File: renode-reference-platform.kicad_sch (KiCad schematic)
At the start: 33 parts, among them J1 USB-C_GCT_USB4105-GF-A, J2 USB-C_GCT_USB4105-GF-A, J3 RJ45_Abracon_ARJM11B1-502-AB-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, J4 Tag-Connect_TC2050-IDC-NL_2x5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, J5 PinSocket_2x6_P2.54mm_Drill1.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, J6 PinSocket_2x6_P2.54mm_Drill1.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, J7 PinSocket_2x20_P2.54mm_Drill1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, J8 JST_SH_1x4_SM04B-SRSS-TB-LF-SN, J9 JST_SH_1x4_SM04B-SRSS-TB-LF-SN, SW1 SW_1301_9305_THT, SW2 SW_1301_9305_THT, SW3 SW_1301_9305_THT, SW4 SW_1301_9305_THT, U1 STM32H753ZIT6, U2 FT2232HL-REEL, U3 IIS2MDCTR, U4 LSM6DSO32TR, U5 TMP108AIYFFR, U6 BME280, U7 AT25FF161A-MAHN-T, U8 INA187A1IDBVR

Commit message: [#94684] Add subsheets
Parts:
- removed D1, D2, D3, D4: LED_G_0402_VLMTG1500-GS08, antmicro-footprints:LED_0402_1005Metric_G, symbol antmicroLEDIndicationDiscrete:LED_G_0402_VLMTG1500-GS08
- removed D5: LED_RGB_2525_LTRBRASF_6B6C-0112-0, antmicro-footprints:LED_RGB_2525Metric_LTRBRASF, symbol antmicroLEDIndicationDiscrete:LED_RGB_2525_LTRBRASF_6B6C-0112-0
- removed J1, J2: USB-C_GCT_USB4105-GF-A, antmicro-footprints:USB-C_Receptacle_GCT_USB4105-GF-A, symbol antmicroUSBConnectors:USB-C_GCT_USB4105-GF-A
- removed J3: RJ45_Abracon_ARJM11B1-502-AB-EW2, antmicro-footprints:RJ45_ARJM11B1-502-AB-EW2_Horizontal, symbol antmicroModularConnectorsJacks:RJ45_Abracon_ARJM11B1-502-AB-EW2
- removed J4: Tag-Connect_TC2050-IDC-NL_2x5_P1.27mm, antmicro-footprints:Tag-Connect_TC2050-IDC-NL_2x5_P1.27mm, symbol antmicroTestPoints:Tag-Connect_TC2050-IDC-NL_2x5_P1.27mm
- removed J5, J6: PinSocket_2x6_P2.54mm_Drill1.04mm_Horizontal, antmicro-footprints:PinSocket_2x6_P2.54mm_Drill1.04mm_Horizontal, symbol antmicroGenericPinSockets:PinSocket_2x6_P2.54mm_Drill1.04mm_Horizontal
- removed J7: PinSocket_2x20_P2.54mm_Drill1.02mm, antmicro-footprints:PinSocket_2x20_P2.54mm_Drill1.02mm, symbol antmicroGenericPinSockets:PinSocket_2x20_P2.54mm_Drill1.02mm
- removed J8, J9: JST_SH_1x4_SM04B-SRSS-TB-LF-SN, antmicro-footprints:Conn_JST_SH_1x4_SM04B-SRSS-TB-LF-SN, symbol antmicroWire2BoardConnectors:JST_SH_1x4_SM04B-SRSS-TB-LF-SN
- removed R1, R2, R3: R_0R_0402, antmicro-footprints:R_0402_1005Metric, symbol antmicroResistors0402:R_0R_0402
- removed SW1, SW2, SW3, SW4: SW_1301_9305_THT, antmicro-footprints:SW_1301_9305_THT, symbol antmicroPushbuttonSwitches:SW_1301_9305_THT
- removed U1: STM32H753ZIT6, antmicro-footprints:LQFP-144_20x20mm_P0.5mm, symbol antmicroMicrocontrollers:STM32H753ZIT6
- removed U2: FT2232HL-REEL, antmicro-footprints:LQFP-64_10x10mm_P0.5mm, symbol antmicroInterfaceControllers:FT2232HL-REEL
- removed U3: IIS2MDCTR, antmicro-footprints:LGA-12_2x2mm_P0.5mm, symbol antmicroMotionSensorsIMUsInertialMeasurementUnits:IIS2MDCTR
- removed U4: LSM6DSO32TR, antmicro-footprints:LGA-14L_3x2.5mm_P0.5mm, symbol antmicroMotionSensorsIMUsInertialMeasurementUnits:LSM6DSO32TR
- removed U5: TMP108AIYFFR, antmicro-footprints:Texas_DSBGA-6_1.2x0.8mm_Layout2x3_P0.4mm, symbol antmicroTemperatureSensorsAnalogandDigitalOutput:TMP108AIYFFR
- removed U6: BME280, antmicro-footprints:LGA-8_2.5x2.5mm_BME280, symbol antmicroHumidityMoistureSensors:BME280
- removed U7: AT25FF161A-MAHN-T, antmicro-footprints:USON-8_2x3mm_P0.5mm, symbol antmicroMemory:AT25FF161A-MAHN-T
- removed U8: INA187A1IDBVR, antmicro-footprints:SOT-23-6, symbol antmicroPowerMeasurement:INA187A1IDBVR
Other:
- added sheet Ethernet (eth.kicad_sch)
- added sheet IMU (imu.kicad_sch)
- added sheet IOs (ios.kicad_sch)
- added sheet MCU (mcu.kicad_sch)
- added sheet PMOD (pmod.kicad_sch)
- added sheet Power (power.kicad_sch)
- added sheet RPI Connector (rpi-expansion.kicad_sch)
- added sheet SPI Flash (spi-flash.kicad_sch)
- added sheet USB-C (usb-c.kicad_sch)
- added sheet USB-C Debug (debug-usb-c.kicad_sch)

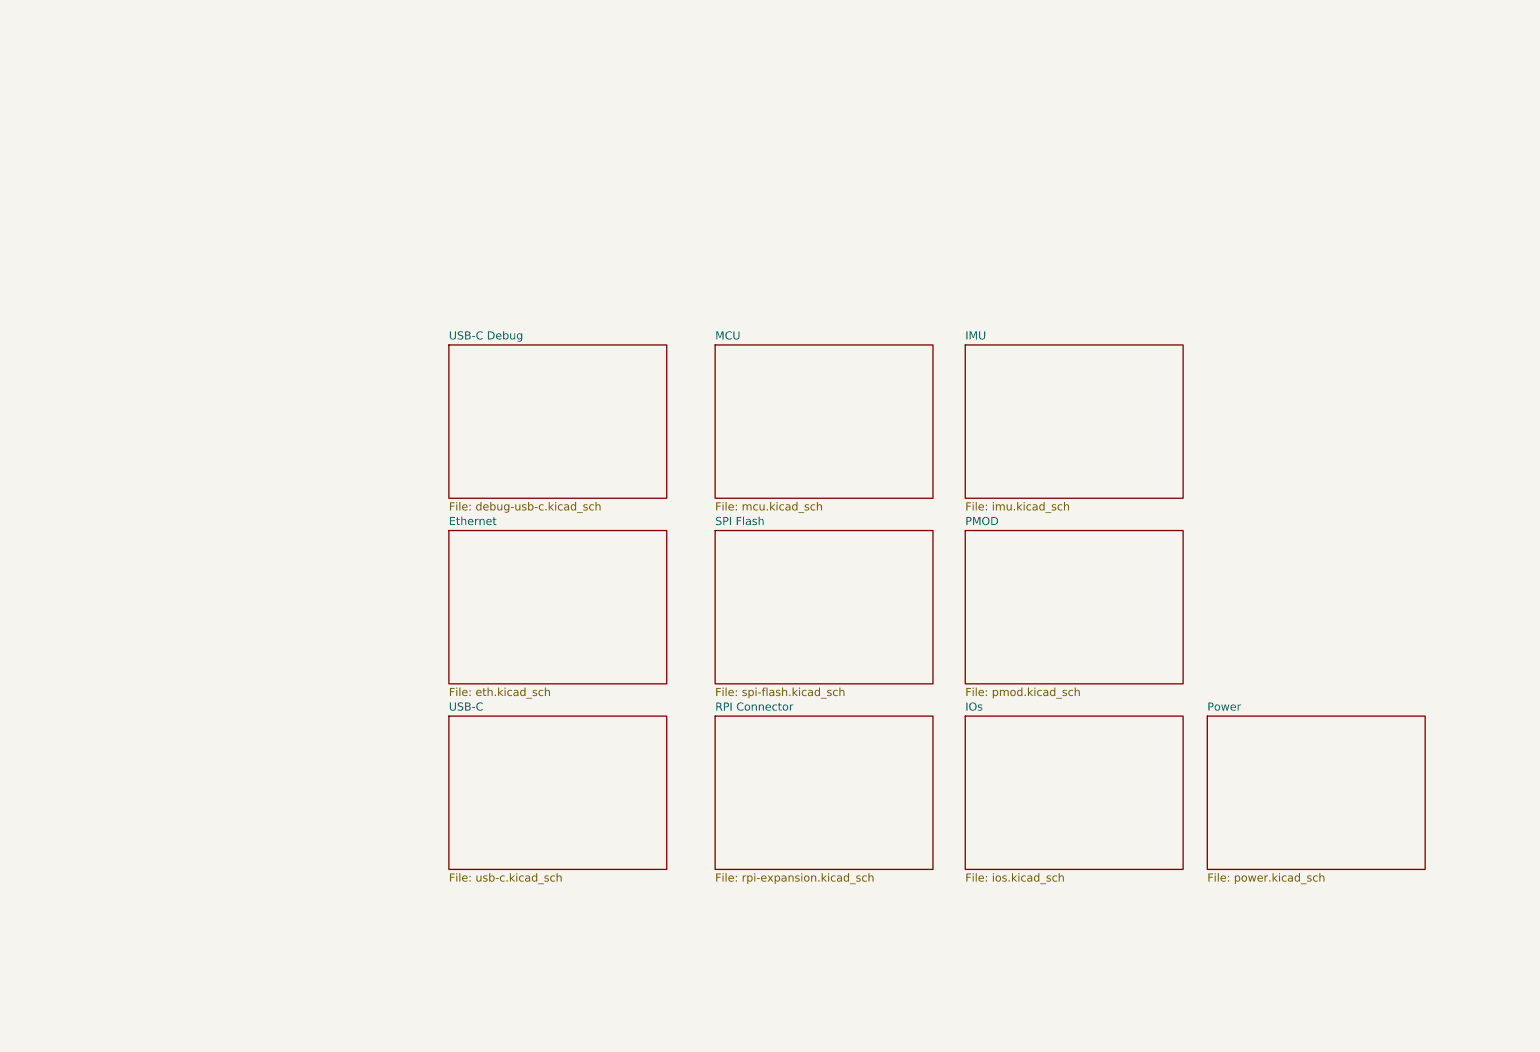
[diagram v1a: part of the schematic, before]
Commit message: [#94684] Add ports to subsheets
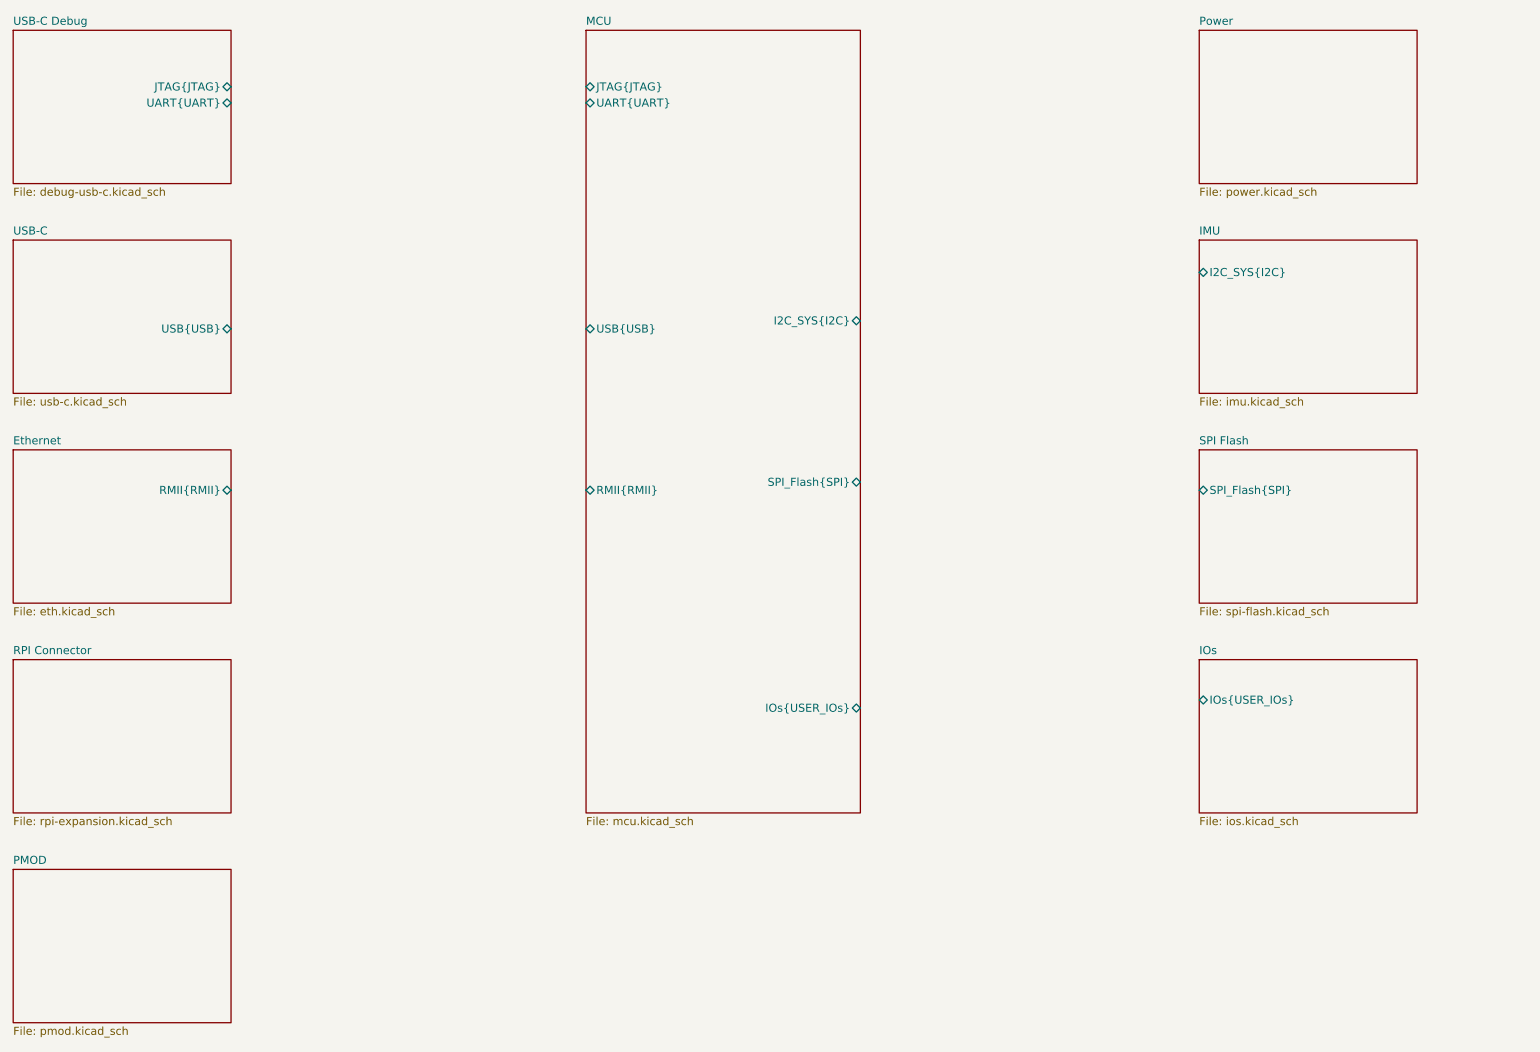
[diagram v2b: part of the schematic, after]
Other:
- sheet Ethernet ports: added RMII{RMII}; removed none
- sheet IMU ports: added I2C_SYS{I2C}; removed none
- sheet IOs ports: added IOs{USER_IOs}; removed none
- sheet MCU ports: added I2C_SYS{I2C}, IOs{USER_IOs}, JTAG{JTAG}, RMII{RMII}, SPI_Flash{SPI}, UART{UART}, USB{USB}; removed none
- sheet SPI Flash ports: added SPI_Flash{SPI}; removed none
- sheet USB-C ports: added USB{USB}; removed none
- sheet USB-C Debug ports: added JTAG{JTAG}, UART{UART}; removed none

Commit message: [#94684] Revise component placement
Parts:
- removed MP1, MP2, MP3, MP4: MP_NPTH_Drill3.2mm, antmicro-footprints:MP_NPTH_Drill3.2mm, symbol antmicroMechanicalParts:MP_NPTH_Drill3.2mm
- added MP1, MP2, MP3, MP4: MP_NPTH_Drill2.7mm, antmicro-footprints:MP_NPTH_Drill2.7mm, symbol antmicroMechanicalParts:MP_NPTH_Drill2.7mm

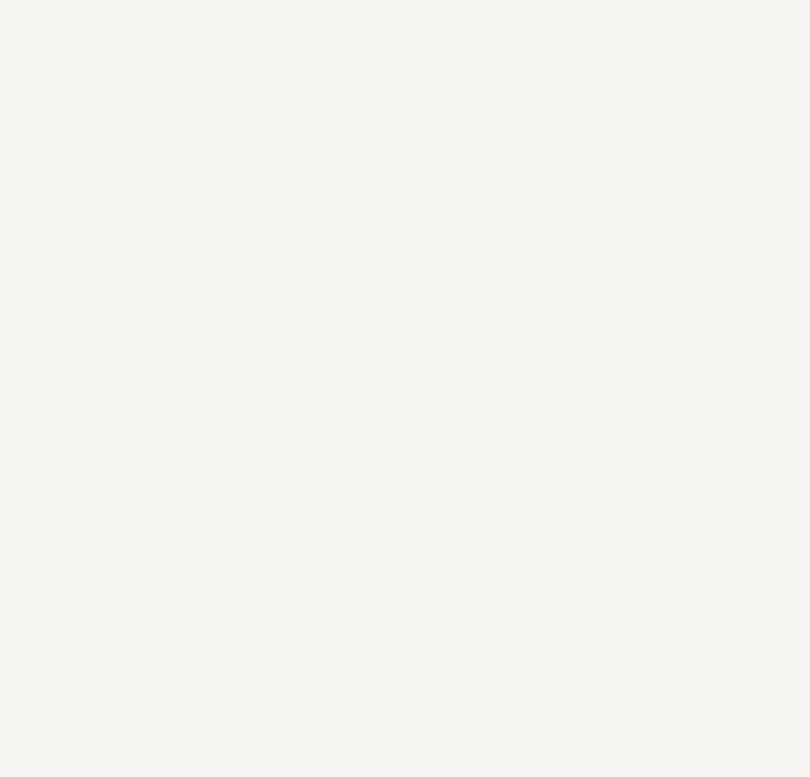
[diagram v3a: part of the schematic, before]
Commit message: [#94620] Add testpoints
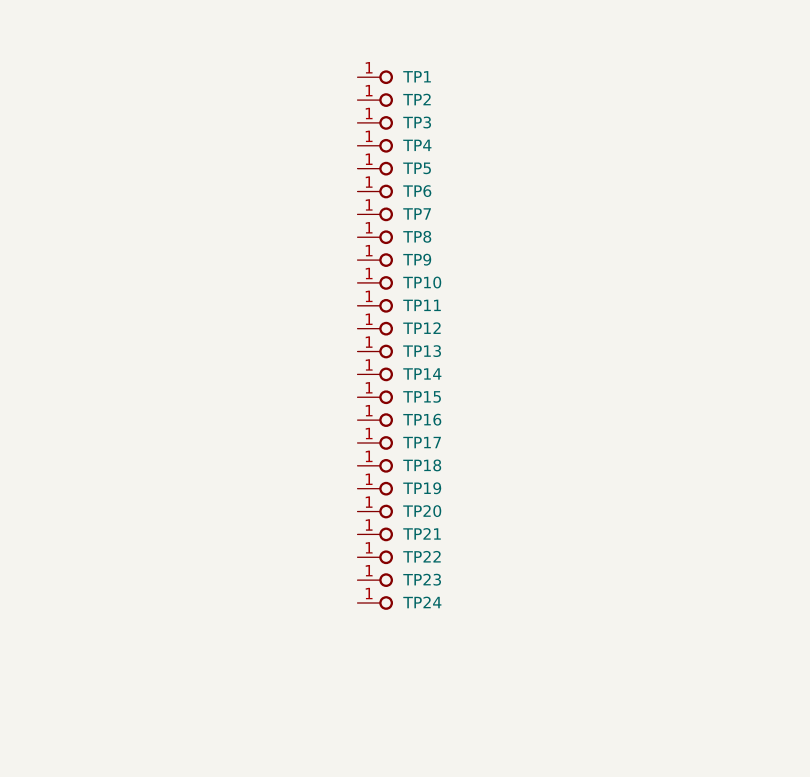
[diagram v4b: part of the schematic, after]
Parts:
- added TP1, TP10, TP11, TP12, TP13, TP14, TP15, TP16, TP17, TP18, TP19, TP2, TP20, TP21, TP22, TP23, TP24, TP3, TP4, TP5, TP6, TP7, TP8, TP9: TP_1.5mm_SMD, antmicro-footprints:TP_SMD_1.5mm, symbol antmicroTestPoints:TP_1.5mm_SMD

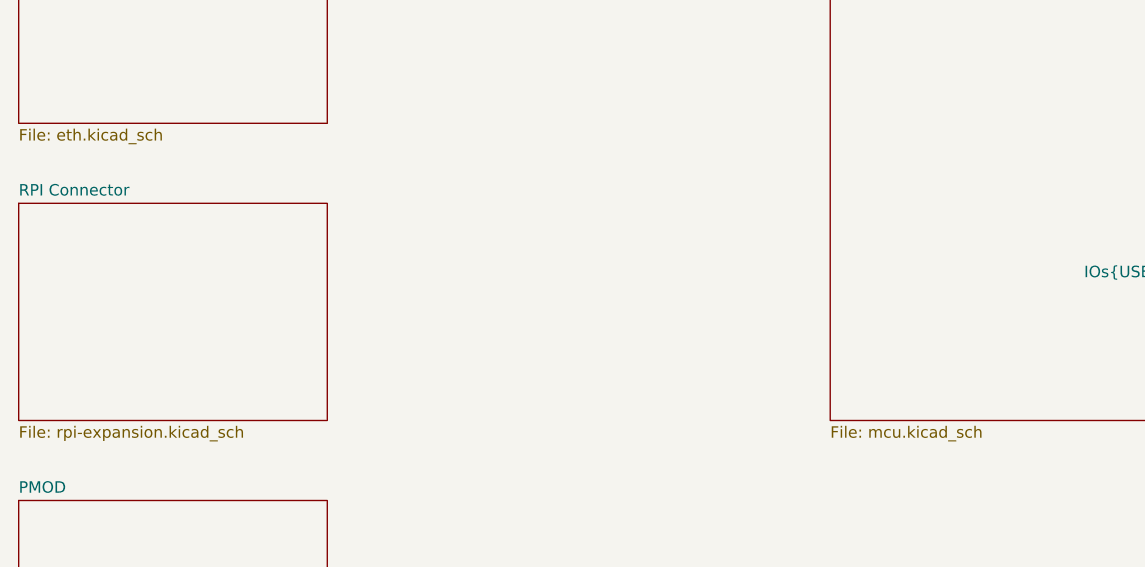
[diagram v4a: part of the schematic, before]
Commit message: [#94727] Add RMII, IOs, JTAG, UART, QSPI connection to MCU
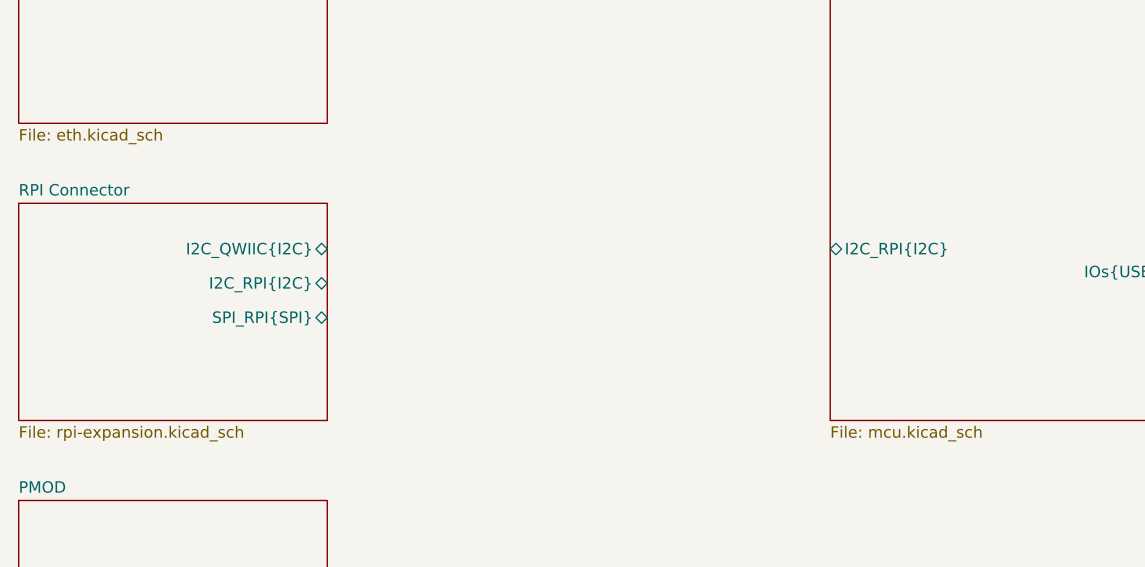
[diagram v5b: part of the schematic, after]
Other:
- sheet MCU ports: added I2C_RPI{I2C}; removed none
- sheet RPI Connector ports: added I2C_QWIIC{I2C}, I2C_RPI{I2C}, SPI_RPI{SPI}; removed none
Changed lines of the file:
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@@
 	)
 	(bus_alias "SPI"
-		(members "MISO" "MOSI" "SCK" "~{CS0}" "~{CS1}")
+		(members "MISO_IO0" "MOSI_IO1" "SCK" "~{CS0}" "~{CS1}" "IO2" "IO3")
 	)
 	(bus_alias "UART"
@@
 			)
 		)
+		(pin "I2C_QWIIC{I2C}" bidirectional
+			(at 99.06 189.23 0)
+			(effects
+				(font
+					(size 1.27 1.27)
+				)
+				(justify right)
+			)
+		)
+		(pin "I2C_RPI{I2C}" bidirectional
+			(at 99.06 193.04 0)
+			(effects
+				(font
+					(size 1.27 1.27)
+				)
+				(justify right)
+			)
+		)
+		(pin "SPI_RPI{SPI}" bidirectional
+			(at 99.06 196.85 0)
+			(effects
+				(font
+					(size 1.27 1.27)
+				)
+				(justify right)
+			)
+		)
 		(instances
 			(project "renode-reference-platform"
@@
 			(effects
 				(font
+					(size 1.27 1.27)
+				)
+				(justify left)
+			)
+		)
+		(pin "I2C_RPI{I2C}" bidirectional
+			(at 154.94 189.23 180)
+			(effects
+				(font

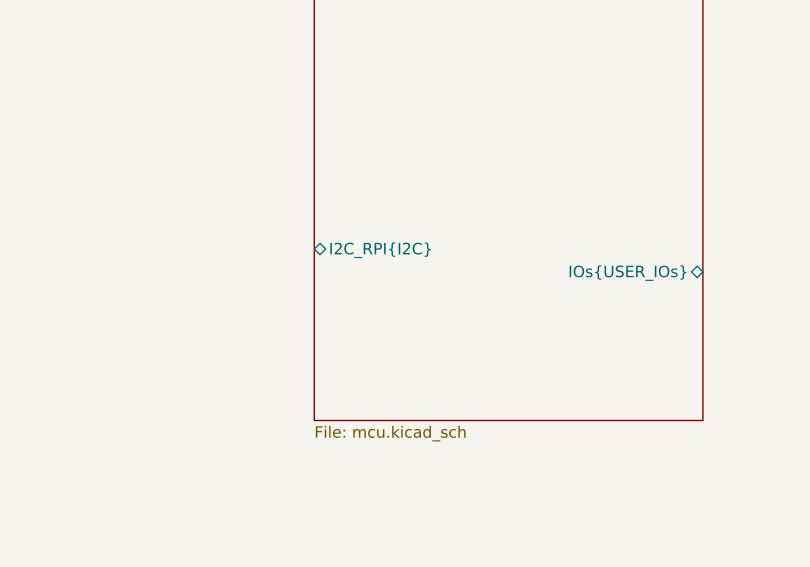
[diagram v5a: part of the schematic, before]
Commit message: [94727] Add remaining I2C buses
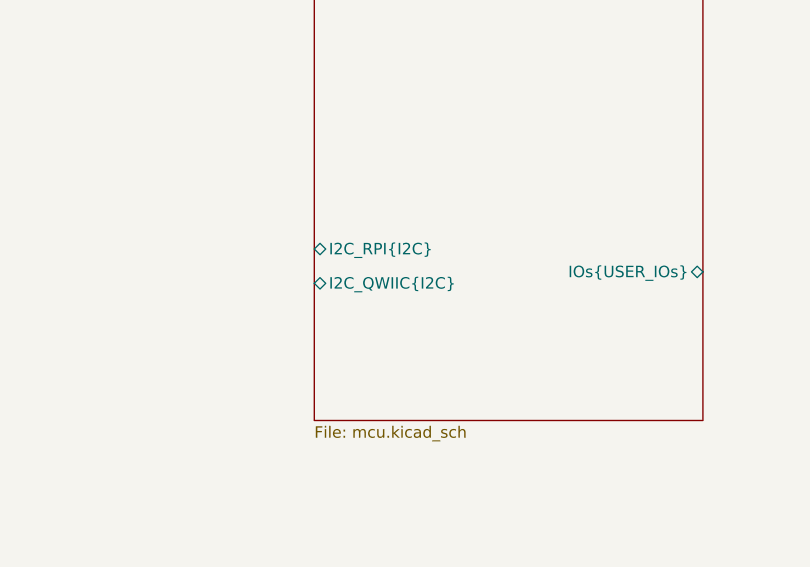
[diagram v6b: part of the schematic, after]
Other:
- sheet MCU ports: added I2C_QWIIC{I2C}; removed none
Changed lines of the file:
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@@
+			)
+		)
+		(pin "I2C_QWIIC{I2C}" bidirectional
+			(at 154.94 193.04 180)
+			(effects
+				(font
+					(size 1.27 1.27)
+				)
+				(justify left)
 			)
 		)
